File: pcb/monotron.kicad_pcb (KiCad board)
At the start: 2 copper layers, 134.6 x 94 mm, 51 parts, among them J1 Mono / Stereo, J10 DIN5-180, J11 DIN5-180, J12 DE9M, J13 DB25_Female, J14 Mini-DIN-6, J15 Mini-DIN-6, J2 Jack-DC, J3 1x7 Header, J4 AudioJack3, J5 DE9F, J6 1x4 Header, J7 DE15HD, J8 2x6 Header, J9 DIN5-180, U1 TM4C123G_Launchpad, U2 MAX3232, U3 74LS14, U4 6N138, U5 ATmega48A-PU

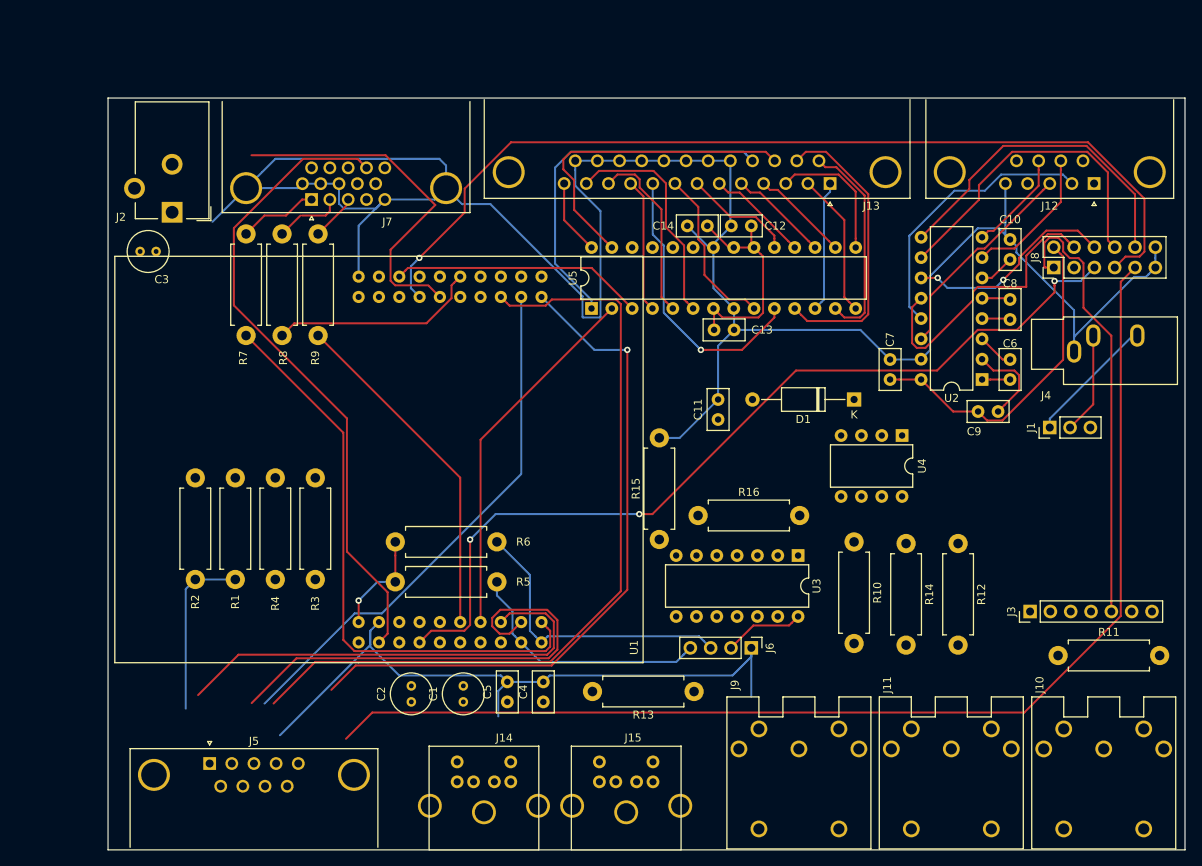
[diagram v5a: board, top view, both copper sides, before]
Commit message: Adjusted component layout again. ) More room between MIDI connectors. ) SD/MMC connector now under Launchpad board
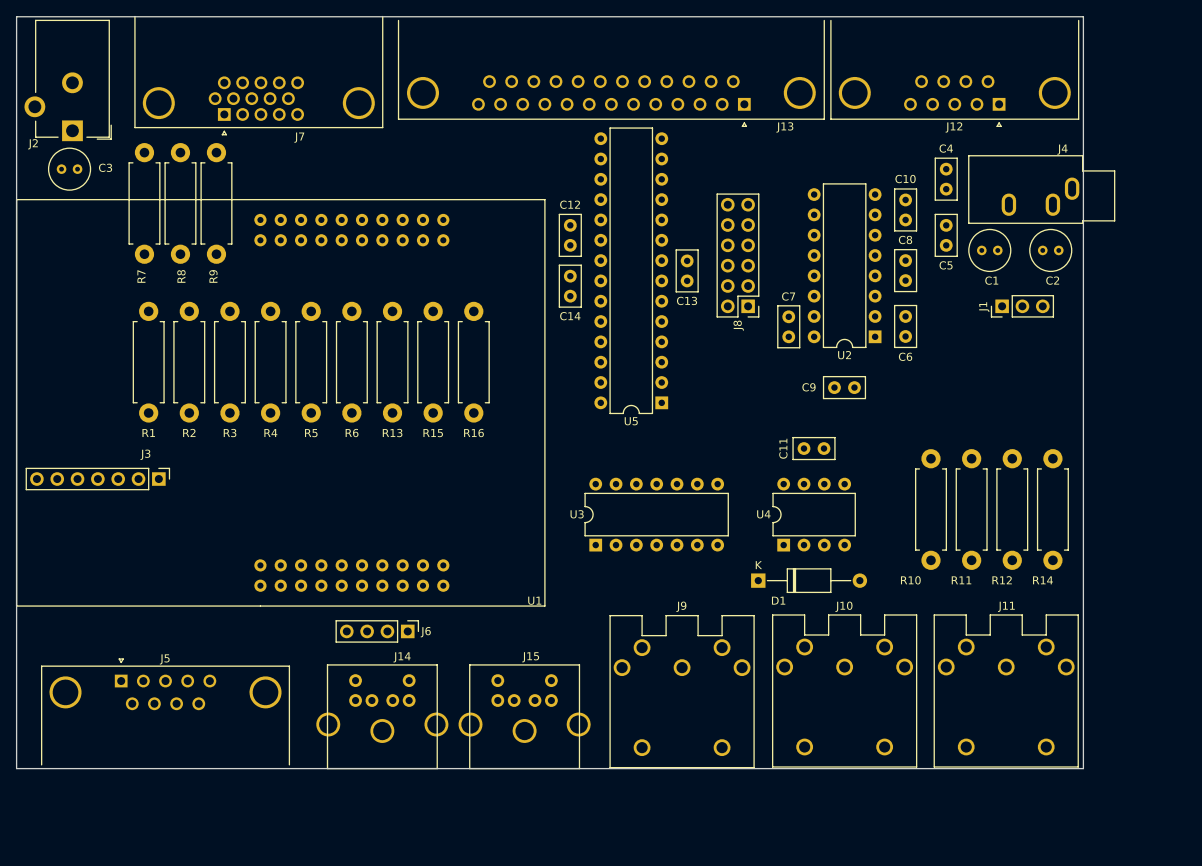
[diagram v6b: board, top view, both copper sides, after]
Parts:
- J10, J11, J9: footprint Launchpad:5P180 DIN Socket -> Monotron:5P180 DIN Socket
- moved J3 110.2 mm to (91.4, 93.3), turned to 270 degrees
- moved C2 97.0 mm to (201.9, 64.8), turned to 0 degrees
- moved C1 85.9 mm to (194.3, 64.8), turned to 0 degrees
- moved C4 83.5 mm to (189.9, 54.6), turned to 270 degrees
- moved C5 79.2 mm to (189.9, 64.1)
- moved R13 51.3 mm to (120.7, 85.1), turned to 90 degrees
- moved J6 43.0 mm to (122.6, 112.4)
- moved R5 41.0 mm to (110.5, 72.4), turned to 270 degrees
- moved J8 38.5 mm to (165.1, 71.8), turned to 180 degrees
- moved J10 34.0 mm to (177.2, 121.8)
- moved R15 32.4 mm to (125.7, 85.1)
- moved R16 30.8 mm to (130.8, 85.1), turned to 90 degrees
- moved D1 25.6 mm to (166.4, 106.0), turned to 0 degrees
- moved U3 25.3 mm to (146.1, 101.6), turned to 90 degrees
- moved R1 23.5 mm to (90.2, 72.4)
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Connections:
- J8 pad 1: +3V3 -> GND
- J8 pad 10: /DTE_CTS -> /PB0_U1RX
- J8 pad 11: GND -> Net-(C7-Pad1)
- J8 pad 12: GND -> +3V3
- J8 pad 2: Net-(C7-Pad1) -> GND
- J8 pad 3: /PB0_U1RX -> /DTE_CTS
- J8 pad 4: /DTE_RX -> /PC5_U1CTS
- J8 pad 5: /PB1_U1TX -> /DTE_RTS
- J8 pad 6: /DTE_TX -> /PC4_U1RTS
- J8 pad 7: /PC4_U1RTS -> /DTE_TX
- J8 pad 8: /DTE_RTS -> /PB1_U1TX
- J8 pad 9: /PC5_U1CTS -> /DTE_RX
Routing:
- net GND: track 387.1 -> 0.00 mm
- net /PC5_U1CTS: track 191.8 -> 0.00 mm
- net /PC4_U1RTS: track 118.2 -> 0.00 mm, vias 1 -> 0
- net /PB1_U1TX: track 110.9 -> 0.00 mm, vias 3 -> 0
- net /PD6_JS_LEFT: track 101.1 -> 0.00 mm
- net /PF4_JS_FIRE: track 85.6 -> 0.00 mm, vias 1 -> 0
- net /PB5_VGA_VSYNC: track 80.8 -> 0.00 mm
- net /PF1_VGA_RED: track 73.3 -> 0.00 mm
- net /PD7_JS_RIGHT: track 66.1 -> 0.00 mm
- net /PE3_JS_DOWN: track 59.4 -> 0.00 mm
- net /PE2_JS_UP: track 57.7 -> 0.00 mm
- net +3V3: track 56.3 -> 0.00 mm
- net +5V: track 51.3 -> 0.00 mm, vias 1 -> 0
- net /PE1_U7TX: track 46.0 -> 0.00 mm
- net /Monotron I/O Expansion/SELPRIN: track 45.4 -> 0.00 mm
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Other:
- board size 134.6 x 94 mm -> 133.3 x 94 mm

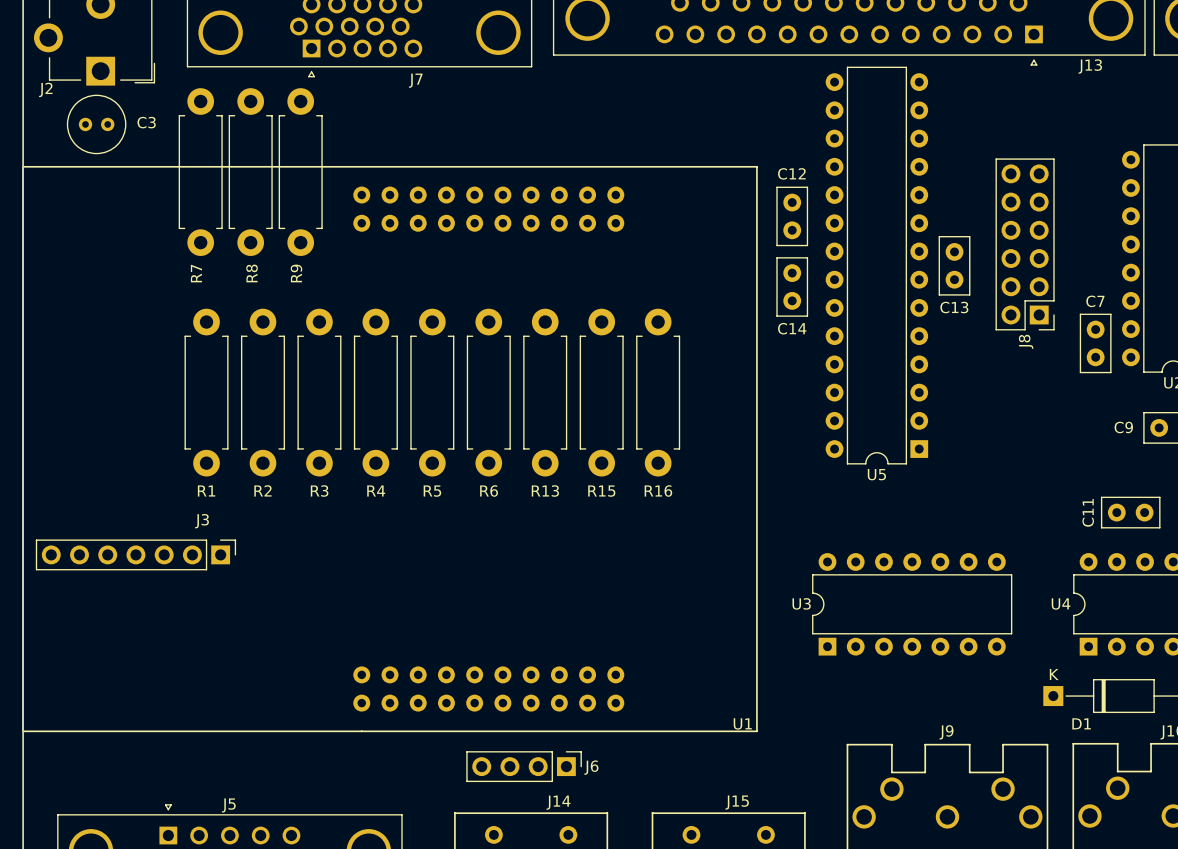
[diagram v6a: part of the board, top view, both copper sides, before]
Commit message: Rotate SD card to match proto-pic board. Shift Launchpad back so you can get to SD card to eject it. Move I2C header to somewhere you can access it.
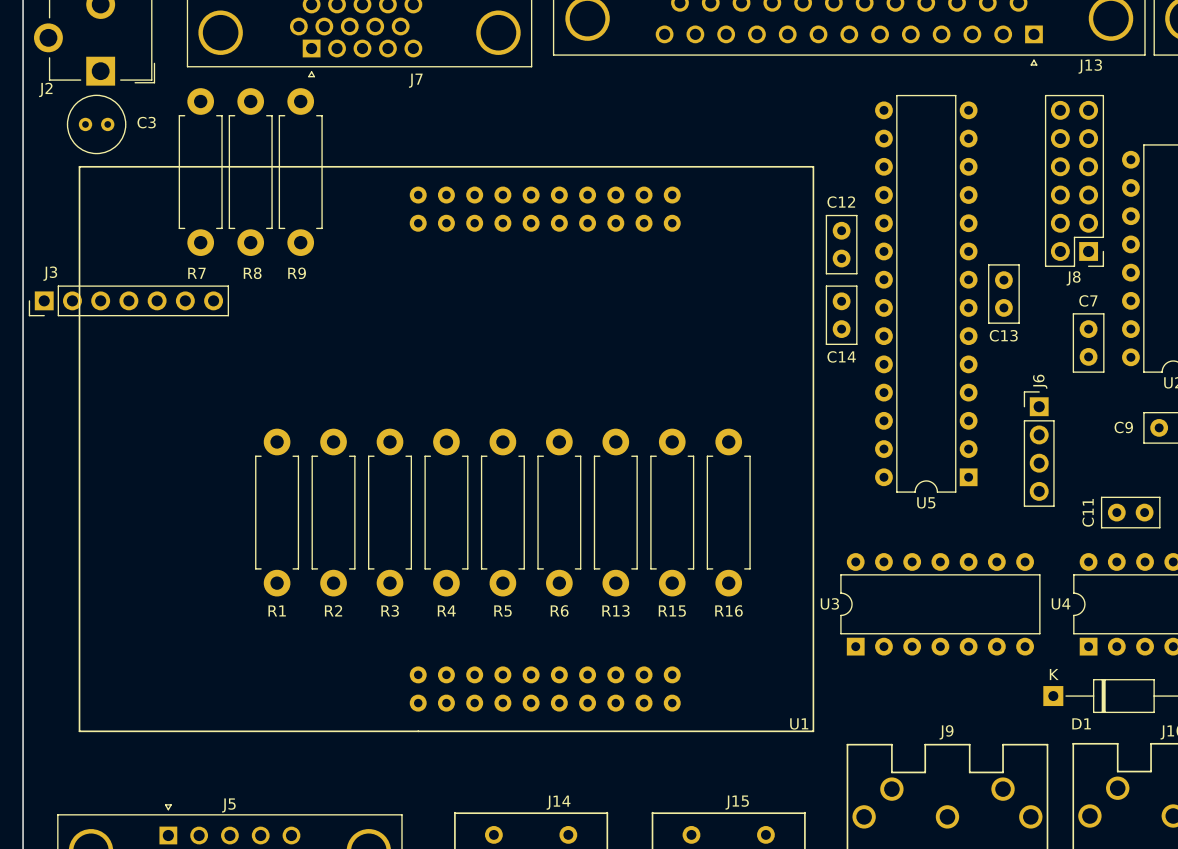
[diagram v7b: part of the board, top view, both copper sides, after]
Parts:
- moved J6 53.5 mm to (165.1, 80.0), turned to 0 degrees
- moved J3 27.8 mm to (75.6, 70.5), turned to 90 degrees
- moved R15 12.5 mm to (132.1, 95.9)
- moved R3 12.5 mm to (106.7, 95.9)
- moved R4 12.5 mm to (111.8, 95.9)
- moved R5 12.5 mm to (116.8, 83.2)
- moved R6 12.5 mm to (121.9, 95.9)
- moved R1 12.5 mm to (96.5, 83.2)
- moved R13 12.5 mm to (127.0, 95.9)
- moved R16 12.5 mm to (137.2, 95.9)
- moved R2 12.5 mm to (101.6, 83.2)
- moved J8 7.24 mm to (169.5, 66.0)
- moved C13 5.12 mm to (161.9, 71.1)
- moved C14 5.12 mm to (147.3, 73.0)
- moved U5 5.12 mm to (158.8, 86.4)
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
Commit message: Finished PCB layout.
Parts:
- moved R5 12.7 mm to (116.8, 95.9), turned to 90 degrees
- moved R6 12.7 mm to (121.9, 83.2), turned to 270 degrees
- moved C5 7.24 mm to (196.8, 66.0)
- moved C1 5.08 mm to (189.2, 64.8)
- moved R1 5.08 mm to (101.6, 83.2)
- moved R2 5.08 mm to (96.5, 83.2)
- moved C4 0.93 mm to (190.5, 55.3)
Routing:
- net GND: track 0.00 -> 400.8 mm
- net +5V: track 0.00 -> 352.9 mm, vias 0 -> 3
- net +3V3: track 0.00 -> 194.9 mm, vias 0 -> 1
- net /PF4_JS_FIRE: track 0.00 -> 146.7 mm
- net Net-(C2-Pad1): track 0.00 -> 131.8 mm, vias 0 -> 3
- net Net-(C1-Pad1): track 0.00 -> 130.0 mm, vias 0 -> 2
- net /PB0_U1RX: track 0.00 -> 108.4 mm, vias 0 -> 3
- net /PD7_JS_RIGHT: track 0.00 -> 106.9 mm
- net /PD6_JS_LEFT: track 0.00 -> 104.3 mm, vias 0 -> 2
- net /PB1_U1TX: track 0.00 -> 102.6 mm
- net /PB4_VGA_HSYNC: track 0.00 -> 100.6 mm, vias 0 -> 3
- net /PA6_I2C_SCL: track 0.00 -> 99.6 mm, vias 0 -> 1
- net /PB5_VGA_VSYNC: track 0.00 -> 97.6 mm, vias 0 -> 1
- net /PE1_U7TX: track 0.00 -> 89.9 mm
- net /PC6_MIDI_IN: track 0.00 -> 86.8 mm, vias 0 -> 1
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- added copper zone on B.Cu, net GND
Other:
- board text added: "3v3"
- board text added: "5V,1A"
- board text added: "CTS"
- board text added: "GND"
- board text added: "I2C Expansion"
- board text added: "Joystick"
- board text added: "KB"
- board text added: "LPT"
- board text added: "Line"
- board text added: "MIDI In"
- board text added: "MIDI Out"
- board text added: "MIDI Thru"
- board text added: "MS"
- board text added: "RS232"
- board text added: "RTS"
- board text added: "RX"
- board text added: "TX"
- board text added: "VGA"
